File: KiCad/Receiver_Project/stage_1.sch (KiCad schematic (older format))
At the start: 10 parts, among them Q1 PN2369A, Q2 2N3904, Q3 2N3904, Q4 2N3904

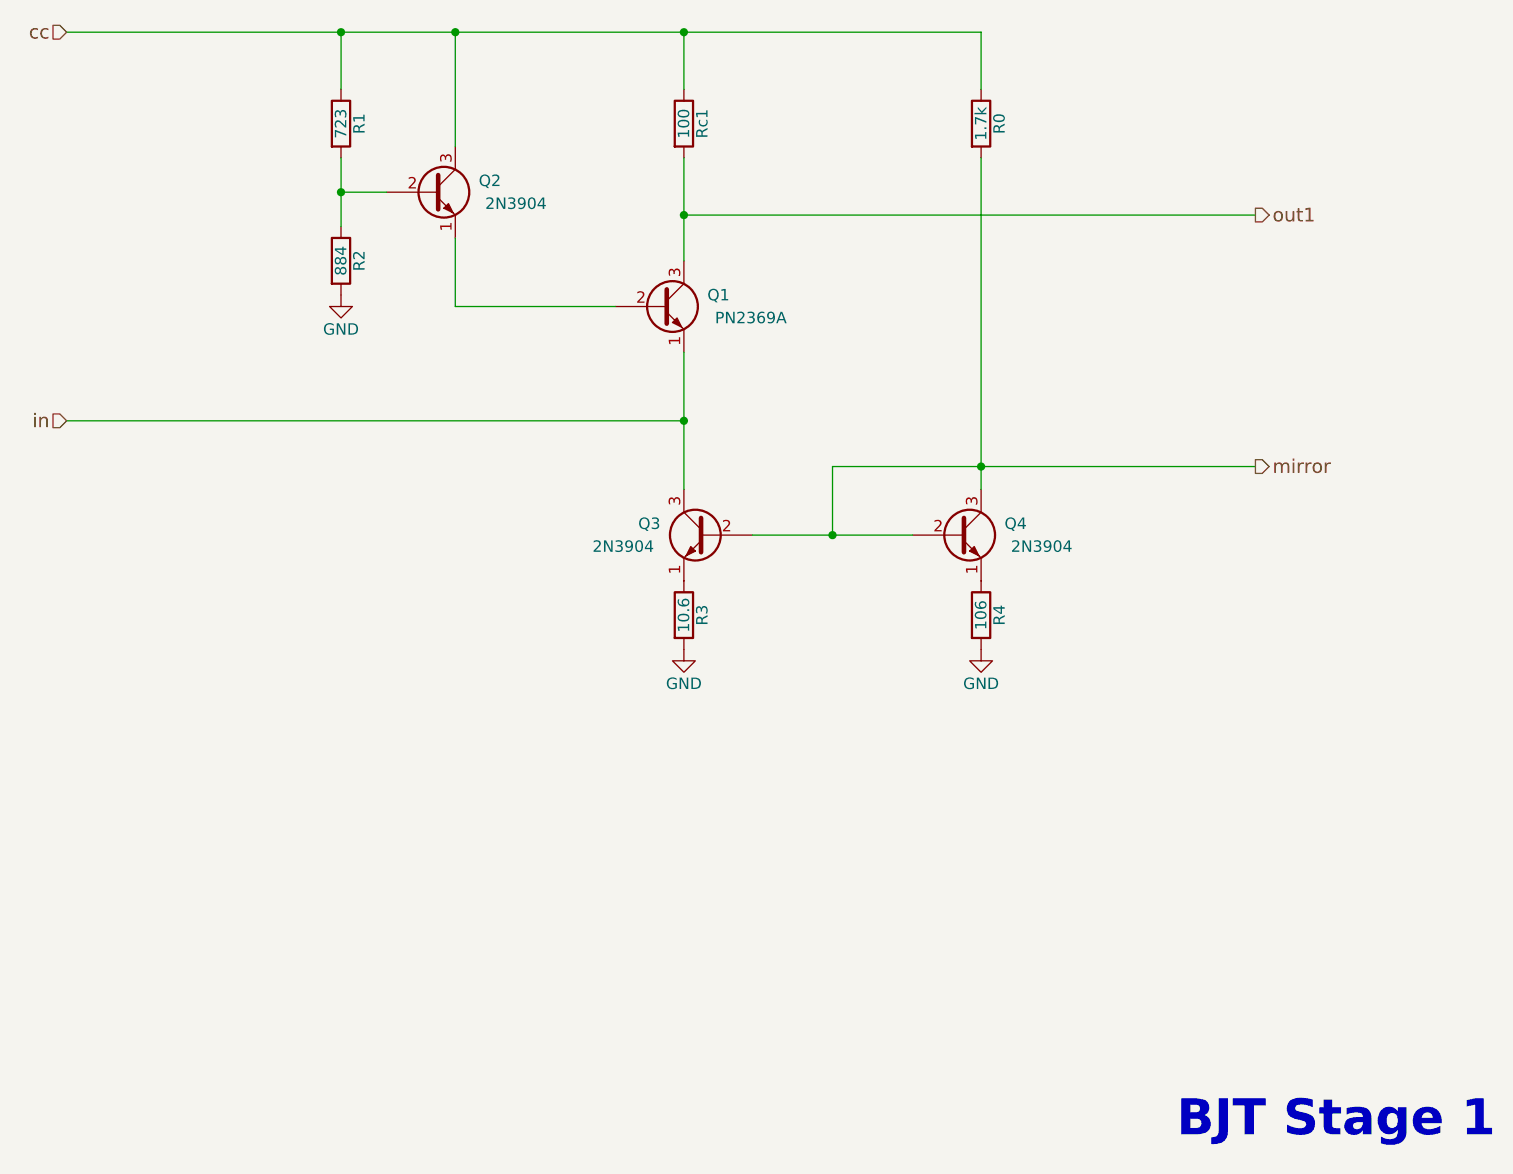
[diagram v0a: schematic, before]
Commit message: added simulation labels to receiver schematic
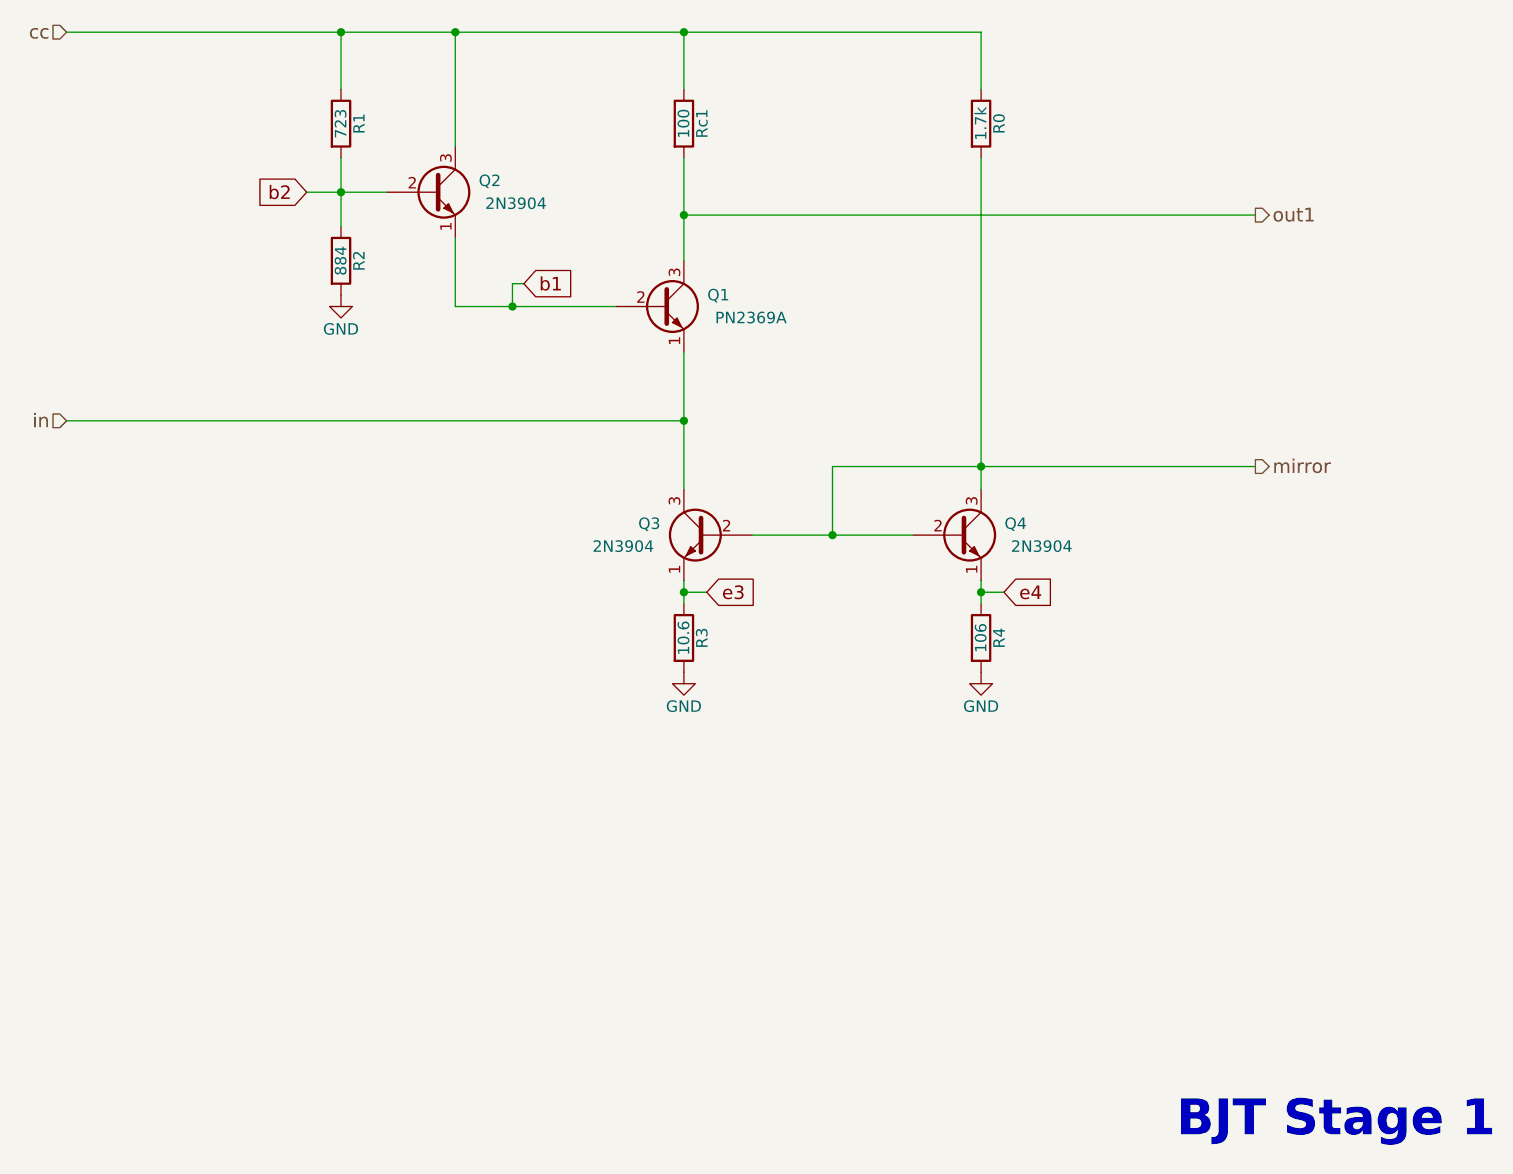
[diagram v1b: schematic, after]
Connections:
- net b1: now reaches Q1.2 (B), Q2.1 (E)
- net b2: now reaches Q2.2 (B), R1.2, R2.1
- net e3: now reaches Q3.1 (E), R3.1
- net e4: now reaches Q4.1 (E), R4.1
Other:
- moved on the sheet: R3, R4
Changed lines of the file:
@@
 L R R3
 U 1 1 56F99C08
-P 5300 4650
-F 0 "R3" V 5380 4650 50  0000 C CNN
-F 1 "10.6" V 5300 4650 50  0000 C CNN
-F 2 "UC_the_Fish_Components:400Mil_Passive" V 5230 4650 50  0001 C CNN
-F 3 "" H 5300 4650 50  0000 C CNN
-	1    5300 4650
+P 5300 4750
+F 0 "R3" V 5380 4750 50  0000 C CNN
+F 1 "10.6" V 5300 4750 50  0000 C CNN
+F 2 "UC_the_Fish_Components:400Mil_Passive" V 5230 4750 50  0001 C CNN
+F 3 "" H 5300 4750 50  0000 C CNN
+	1    5300 4750
 	1    0    0    -1
 $EndComp
@@
 L R R4
 U 1 1 56F99C53
-P 6600 4650
-F 0 "R4" V 6680 4650 50  0000 C CNN
-F 1 "106" V 6600 4650 50  0000 C CNN
-F 2 "UC_the_Fish_Components:400Mil_Passive" V 6530 4650 50  0001 C CNN
-F 3 "" H 6600 4650 50  0000 C CNN
-	1    6600 4650
+P 6600 4750
+F 0 "R4" V 6680 4750 50  0000 C CNN
+F 1 "106" V 6600 4750 50  0000 C CNN
+F 2 "UC_the_Fish_Components:400Mil_Passive" V 6530 4750 50  0001 C CNN
+F 3 "" H 6600 4750 50  0000 C CNN
+	1    6600 4750
 	1    0    0    -1
 $EndComp
@@
 	3800 2650 3800 2950
 Wire Wire Line
-	4000 2800 3800 2800
+	3650 2800 4000 2800
 Connection ~ 3800 2800
 Wire Wire Line
@@
 L GND #PWR026
 U 1 1 56F9ADEC
-P 5300 4800
-F 0 "#PWR026" H 5300 4550 50  0001 C CNN
-F 1 "GND" H 5300 4650 50  0000 C CNN
-F 2 "" H 5300 4800 50  0000 C CNN
-F 3 "" H 5300 4800 50  0000 C CNN
-	1    5300 4800
+P 5300 4900
+F 0 "#PWR026" H 5300 4650 50  0001 C CNN
+F 1 "GND" H 5300 4750 50  0000 C CNN
+F 2 "" H 5300 4900 50  0000 C CNN
+F 3 "" H 5300 4900 50  0000 C CNN
+	1    5300 4900
 	1    0    0    -1
 $EndComp
@@
 L GND #PWR027
 U 1 1 56F9AE64
-P 6600 4800
-F 0 "#PWR027" H 6600 4550 50  0001 C CNN
-F 1 "GND" H 6600 4650 50  0000 C CNN
-F 2 "" H 6600 4800 50  0000 C CNN
-F 3 "" H 6600 4800 50  0000 C CNN
-	1    6600 4800
+P 6600 4900
+F 0 "#PWR027" H 6600 4650 50  0001 C CNN
+F 1 "GND" H 6600 4750 50  0000 C CNN
+F 2 "" H 6600 4900 50  0000 C CNN
+F 3 "" H 6600 4900 50  0000 C CNN
+	1    6600 4900
 	1    0    0    -1
 $EndComp
 Text Notes 8850 6950 2    157  ~ 31
 BJT Stage 1
+Text GLabel 3650 2800 0    59   Input ~ 0
+b2
+Text GLabel 4600 3200 2    59   Input ~ 0
+b1
+Wire Wire Line
+	4600 3200 4550 3200
+Wire Wire Line
+	4550 3200 4550 3300
+Connection ~ 4550 3300
+Wire Wire Line
+	5300 4500 5300 4600
+Text GLabel 5400 4550 2    59   Input ~ 0
+e3
+Wire Wire Line
+	5400 4550 5300 4550
+Connection ~ 5300 4550
+Wire Wire Line
+	6600 4500 6600 4600
+Wire Wire Line
+	6600 4550 6700 4550
+Connection ~ 6600 4550
+Text GLabel 6700 4550 2    59   Input ~ 0
+e4
 $EndSCHEMATC
